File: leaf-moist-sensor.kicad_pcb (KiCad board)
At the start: 2 copper layers, 61 x 70.8 mm, 2 parts, among them P1 CONN_01X02

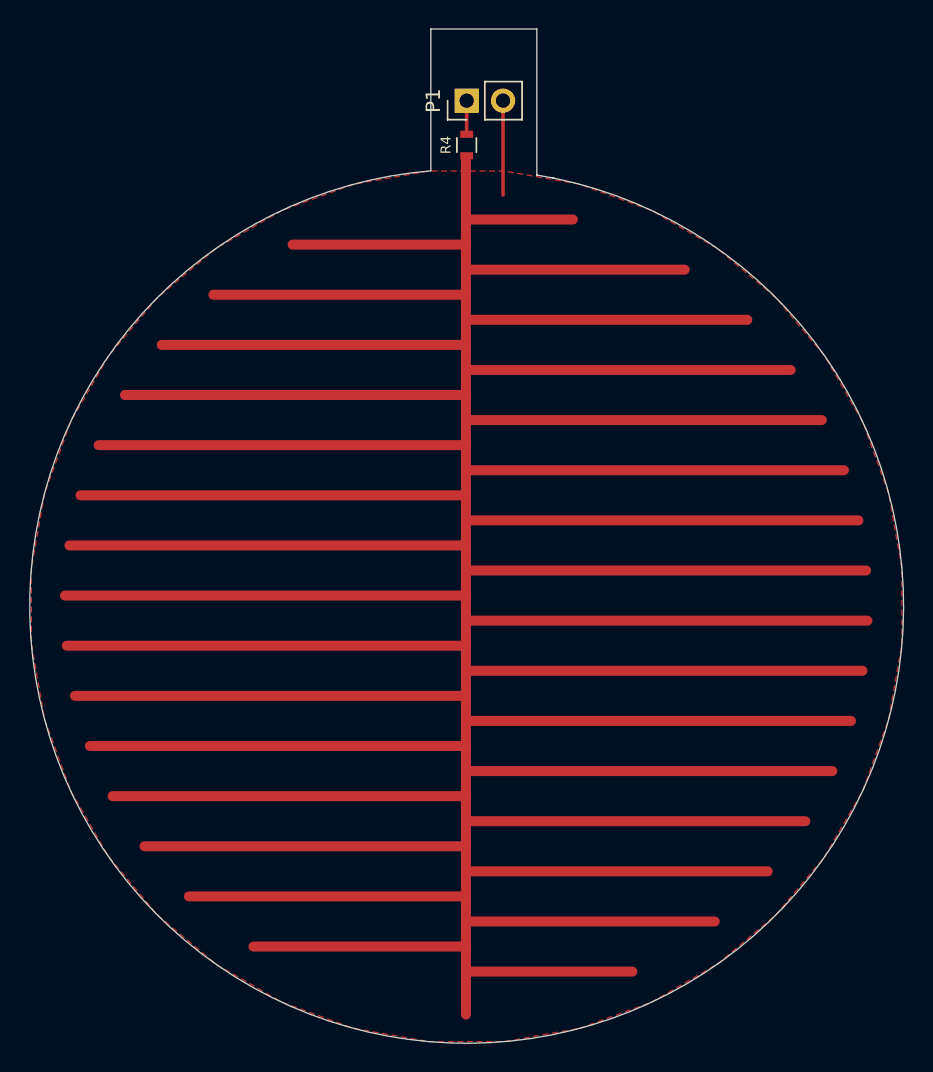
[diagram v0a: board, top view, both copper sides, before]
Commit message: 0.5mm Clearance
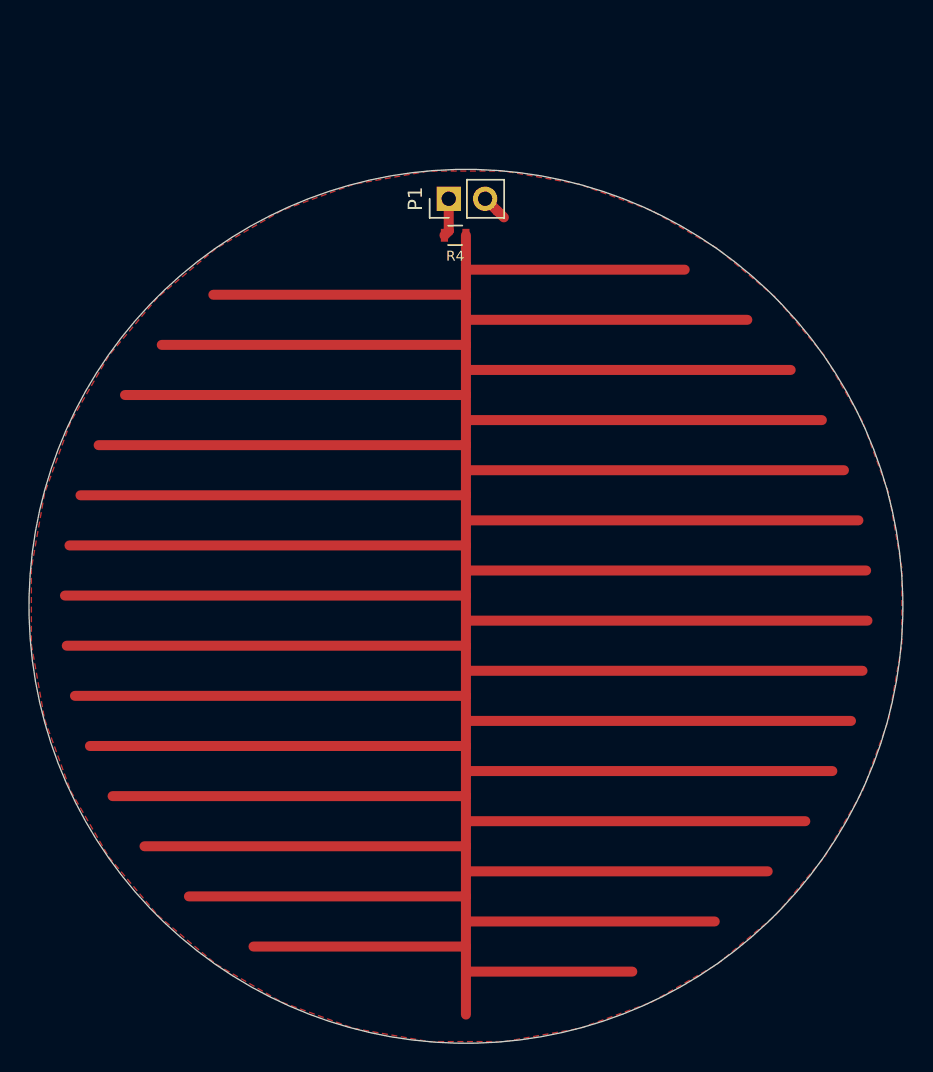
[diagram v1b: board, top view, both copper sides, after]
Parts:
- moved P1 6.96 mm to (132.8, 57.9)
- moved R4 6.35 mm to (133.3, 60.4), turned to 180 degrees
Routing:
- net /SENSOR_TRACK: track 758.2 -> 733.3 mm
- net GND: track 6.59 -> 1.85 mm
- net /EXCITATION: track 2.35 -> 3.10 mm
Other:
- board size 61 x 70.8 mm -> 61 x 61 mm
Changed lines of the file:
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@@
   (general
     (thickness 1.6)
-    (drawings 5)
-    (tracks 34)
+    (drawings 1)
+    (tracks 37)
     (zones 0)
     (modules 2)
@@
   )
   (setup
-    (last_trace_width 0.25)
+    (last_trace_width 0.7)
+    (user_trace_width 0.7)
     (trace_clearance 0.2)
     (zone_clearance 0.508)
@@
   )
   (module Resistors_SMD:R_0603 (layer F.Cu)
-    (at 134.1 54.1 90)
+    (at 133.3 60.4 180)
     (descr "Resistor SMD 0603, reflow soldering, Vishay (see dcrcw.pdf)")
     (tags "resistor 0603")
     (attr smd)
-    (fp_text reference R4 (at 0 -1.45 90) (layer F.SilkS)
+    (fp_text reference R4 (at 0 -1.45 180) (layer F.SilkS)
       (effects (font (size 0.7 0.7) (thickness 0.11)))
     )
-    (fp_text value 330 (at 0 1.5 90) (layer F.Fab) hide
+    (fp_text value 330 (at 0 1.5 180) (layer F.Fab) hide
       (effects (font (size 0.7 0.7) (thickness 0.11)))
     )
@@
     (fp_line (start 0.8 0.4) (end -0.8 0.4) (layer F.Fab) (width 0.1))
     (fp_line (start -0.8 0.4) (end -0.8 -0.4) (layer F.Fab) (width 0.1))
-    (fp_text user %R (at 0 0 90) (layer F.Fab) hide
+    (fp_text user %R (at 0 0 180) (layer F.Fab) hide
       (effects (font (size 0.4 0.4) (thickness 0.075)))
     )
-    (pad 2 smd rect (at 0.75 0 90) (size 0.5 0.9) (layers F.Cu F.Paste F.Mask)
+    (pad 2 smd rect (at 0.75 0 180) (size 0.5 0.9) (layers F.Cu F.Paste F.Mask)
       (net 1 /EXCITATION))
-    (pad 1 smd rect (at -0.75 0 90) (size 0.5 0.9) (layers F.Cu F.Paste F.Mask)
+    (pad 1 smd rect (at -0.75 0 180) (size 0.5 0.9) (layers F.Cu F.Paste F.Mask)
       (net 2 /SENSOR_TRACK))
     (model "${KIPRJMOD}/3d/User Library-RES_SMD-1.STEP"
@@
   )
   (module Pin_Headers:Pin_Header_Straight_1x02_Pitch2.54mm (layer F.Cu)
-    (at 134.1 51 90)
+    (at 132.85 57.85 90)
     (descr "Through hole straight pin header, 1x02, 2.54mm pitch, single row")
     (tags "Through hole pin header THT 1x02 2.54mm single row")
@@
       (effects (font (size 1 1) (thickness 0.15)))
     )
-    (fp_text value CONN_01X02 (at 0 4.87 90) (layer F.Fab)
+    (fp_text value CONN_01X02 (at 0 4.87 90) (layer F.Fab) hide
       (effects (font (size 1 1) (thickness 0.15)))
     )
+    (fp_line (start 1.8 -1.8) (end -1.8 -1.8) (layer F.CrtYd) (width 0.05))
+    (fp_line (start 1.8 4.35) (end 1.8 -1.8) (layer F.CrtYd) (width 0.05))
+    (fp_line (start -1.8 4.35) (end 1.8 4.35) (layer F.CrtYd) (width 0.05))
+    (fp_line (start -1.8 -1.8) (end -1.8 4.35) (layer F.CrtYd) (width 0.05))
+    (fp_line (start -1.33 -1.33) (end 0 -1.33) (layer F.SilkS) (width 0.12))
+    (fp_line (start -1.33 0) (end -1.33 -1.33) (layer F.SilkS) (width 0.12))
+    (fp_line (start -1.33 1.27) (end 1.33 1.27) (layer F.SilkS) (width 0.12))
+    (fp_line (start 1.33 1.27) (end 1.33 3.87) (layer F.SilkS) (width 0.12))
+    (fp_line (start -1.33 1.27) (end -1.33 3.87) (layer F.SilkS) (width 0.12))
+    (fp_line (start -1.33 3.87) (end 1.33 3.87) (layer F.SilkS) (width 0.12))
+    (fp_line (start -1.27 -0.635) (end -0.635 -1.27) (layer F.Fab) (width 0.1))
+    (fp_line (start -1.27 3.81) (end -1.27 -0.635) (layer F.Fab) (width 0.1))
+    (fp_line (start 1.27 3.81) (end -1.27 3.81) (layer F.Fab) (width 0.1))
+    (fp_line (start 1.27 -1.27) (end 1.27 3.81) (layer F.Fab) (width 0.1))
     (fp_line (start -0.635 -1.27) (end 1.27 -1.27) (layer F.Fab) (width 0.1))
-    (fp_line (start 1.27 -1.27) (end 1.27 3.81) (layer F.Fab) (width 0.1))
-    (fp_line (start 1.27 3.81) (end -1.27 3.81) (layer F.Fab) (width 0.1))
-    (fp_line (start -1.27 3.81) (end -1.27 -0.635) (layer F.Fab) (width 0.1))
-    (fp_line (start -1.27 -0.635) (end -0.635 -1.27) (layer F.Fab) (width 0.1))
-    (fp_line (start -1.33 3.87) (end 1.33 3.87) (layer F.SilkS) (width 0.12))
-    (fp_line (start -1.33 1.27) (end -1.33 3.87) (layer F.SilkS) (width 0.12))
-    (fp_line (start 1.33 1.27) (end 1.33 3.87) (layer F.SilkS) (width 0.12))
-    (fp_line (start -1.33 1.27) (end 1.33 1.27) (layer F.SilkS) (width 0.12))
-    (fp_line (start -1.33 0) (end -1.33 -1.33) (layer F.SilkS) (width 0.12))
-    (fp_line (start -1.33 -1.33) (end 0 -1.33) (layer F.SilkS) (width 0.12))
-    (fp_line (start -1.8 -1.8) (end -1.8 4.35) (layer F.CrtYd) (width 0.05))
-    (fp_line (start -1.8 4.35) (end 1.8 4.35) (layer F.CrtYd) (width 0.05))
-    (fp_line (start 1.8 4.35) (end 1.8 -1.8) (layer F.CrtYd) (width 0.05))
-    (fp_line (start 1.8 -1.8) (end -1.8 -1.8) (layer F.CrtYd) (width 0.05))
+    (pad 2 thru_hole oval (at 0 2.54 90) (size 1.7 1.7) (drill 1) (layers *.Cu *.Mask)
+      (net 3 GND))
     (pad 1 thru_hole rect (at 0 0 90) (size 1.7 1.7) (drill 1) (layers *.Cu *.Mask)
       (net 1 /EXCITATION))
-    (pad 2 thru_hole oval (at 0 2.54 90) (size 1.7 1.7) (drill 1) (layers *.Cu *.Mask)
-      (net 3 GND))
     (model ${KISYS3DMOD}/Pin_Headers.3dshapes/Pin_Header_Straight_1x02_Pitch2.54mm.wrl
       (at (xyz 0 0 0))
@@
     )
   )
-  (gr_line (start 139 46) (end 139 56.2) (layer Edge.Cuts) (width 0.05))
-  (gr_line (start 131.6 46) (end 139 46) (layer Edge.Cuts) (width 0.05))
-  (gr_line (start 131.6 55.9) (end 131.6 46) (layer Edge.Cuts) (width 0.05))
-  (gr_line (start 140.1 56.4) (end 140.2 56.4) (layer Edge.Cuts) (width 0.05))
-  (gr_arc (start 134.1 86.3) (end 131.6 55.9) (angle -346.0827353) (layer Edge.Cuts) (width 0.05))
-  (segment (start 134.1 53.35) (end 134.1 51) (width 0.25) (layer F.Cu) (net 1))
-  (segment (start 134.05 55) (end 134.05 114.8) (width 0.7) (layer F.Cu) (net 2))
-  (segment (start 134.1 59.3) (end 141.516198 59.3) (width 0.7) (layer F.Cu) (net 2))
+  (gr_circle (center 134.05 86.3) (end 134.05 55.8) (layer Edge.Cuts) (width 0.05))
+  (segment (start 132.55 57.55) (end 132.85 57.25) (width 0.25) (layer F.Cu) (net 1))
+  (segment (start 132.85 60.1) (end 132.55 60.4) (width 0.7) (layer F.Cu) (net 1))
+  (segment (start 132.85 57.85) (end 132.85 60.1) (width 0.7) (layer F.Cu) (net 1))
+  (segment (start 134.05 62.5) (end 134.05 114.8) (width 0.7) (layer F.Cu) (net 2))
   (segment (start 134.1 62.8) (end 149.323337 62.8) (width 0.7) (layer F.Cu) (net 2))
   (segment (start 134.1 66.3) (end 153.695918 66.3) (width 0.7) (layer F.Cu) (net 2))
@@
   (segment (start 134.1 108.3) (end 151.420508 108.3) (width 0.7) (layer F.Cu) (net 2))
   (segment (start 134.1 111.8) (end 145.665034 111.8) (width 0.7) (layer F.Cu) (net 2))
-  (segment (start 134.05 61.05) (end 121.948864 61.05) (width 0.7) (layer F.Cu) (net 2))
   (segment (start 134.05 64.55) (end 116.41658 64.55) (width 0.7) (layer F.Cu) (net 2))
   (segment (start 134.05 68.05) (end 112.814711 68.05) (width 0.7) (layer F.Cu) (net 2))
@@
   (segment (start 134.05 106.55) (end 114.712536 106.55) (width 0.7) (layer F.Cu) (net 2))
   (segment (start 134.05 110.05) (end 119.21971 110.05) (width 0.7) (layer F.Cu) (net 2))
-  (segment (start 136.64 51) (end 136.64 57.59) (width 0.25) (layer F.Cu) (net 3))
+  (segment (start 134.05 60.4) (end 134.05 62.5) (width 0.7) (layer F.Cu) (net 2))
+  (segment (start 136.239999 58.699999) (end 136.249999 58.699999) (width 0.7) (layer F.Cu) (net 3))
+  (segment (start 135.39 57.85) (end 136.239999 58.699999) (width 0.7) (layer F.Cu) (net 3))
+  (segment (start 136.249999 58.699999) (end 136.7 59.15) (width 0.7) (layer F.Cu) (net 3))
   (zone (net 3) (net_name GND) (layer F.Cu) (hatch edge 0.508)
     (connect_pads (clearance 0.508))
@@
       )
     )
+  )
+  (zone (net 0) (net_name "") (layer F.Cu) (hatch edge 0.508)
+    (connect_pads (clearance 0.508))
+    (min_thickness 0.254)
+    (keepout (tracks allowed) (vias allowed) (copperpour not_allowed))
+    (fill (arc_segments 16) (thermal_gap 0.508) (thermal_bridge_width 0.508))
+    (polygon
+      (pts
+        (xy 135.05 55.8) (xy 135.05 61.95) (xy 127.6 61.95) (xy 129.1 55.8)
+      )
+    )
